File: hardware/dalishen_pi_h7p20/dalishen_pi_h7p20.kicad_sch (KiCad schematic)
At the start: 100 parts, among them J1 Conn_02x05_Odd_Even, J6 5V, J7 OV5640, J9 D500C930SV0, SW1 SW_Push, SW2 SW_Push, SW3 SW_DIP_x03, U3 H7P20N0L128-M3H1, U4 SY7201ABC, U5 XC6206-2.8, U7 P25Q32SH-SSH-IT, U8 XC6206-1.5, X1 NC

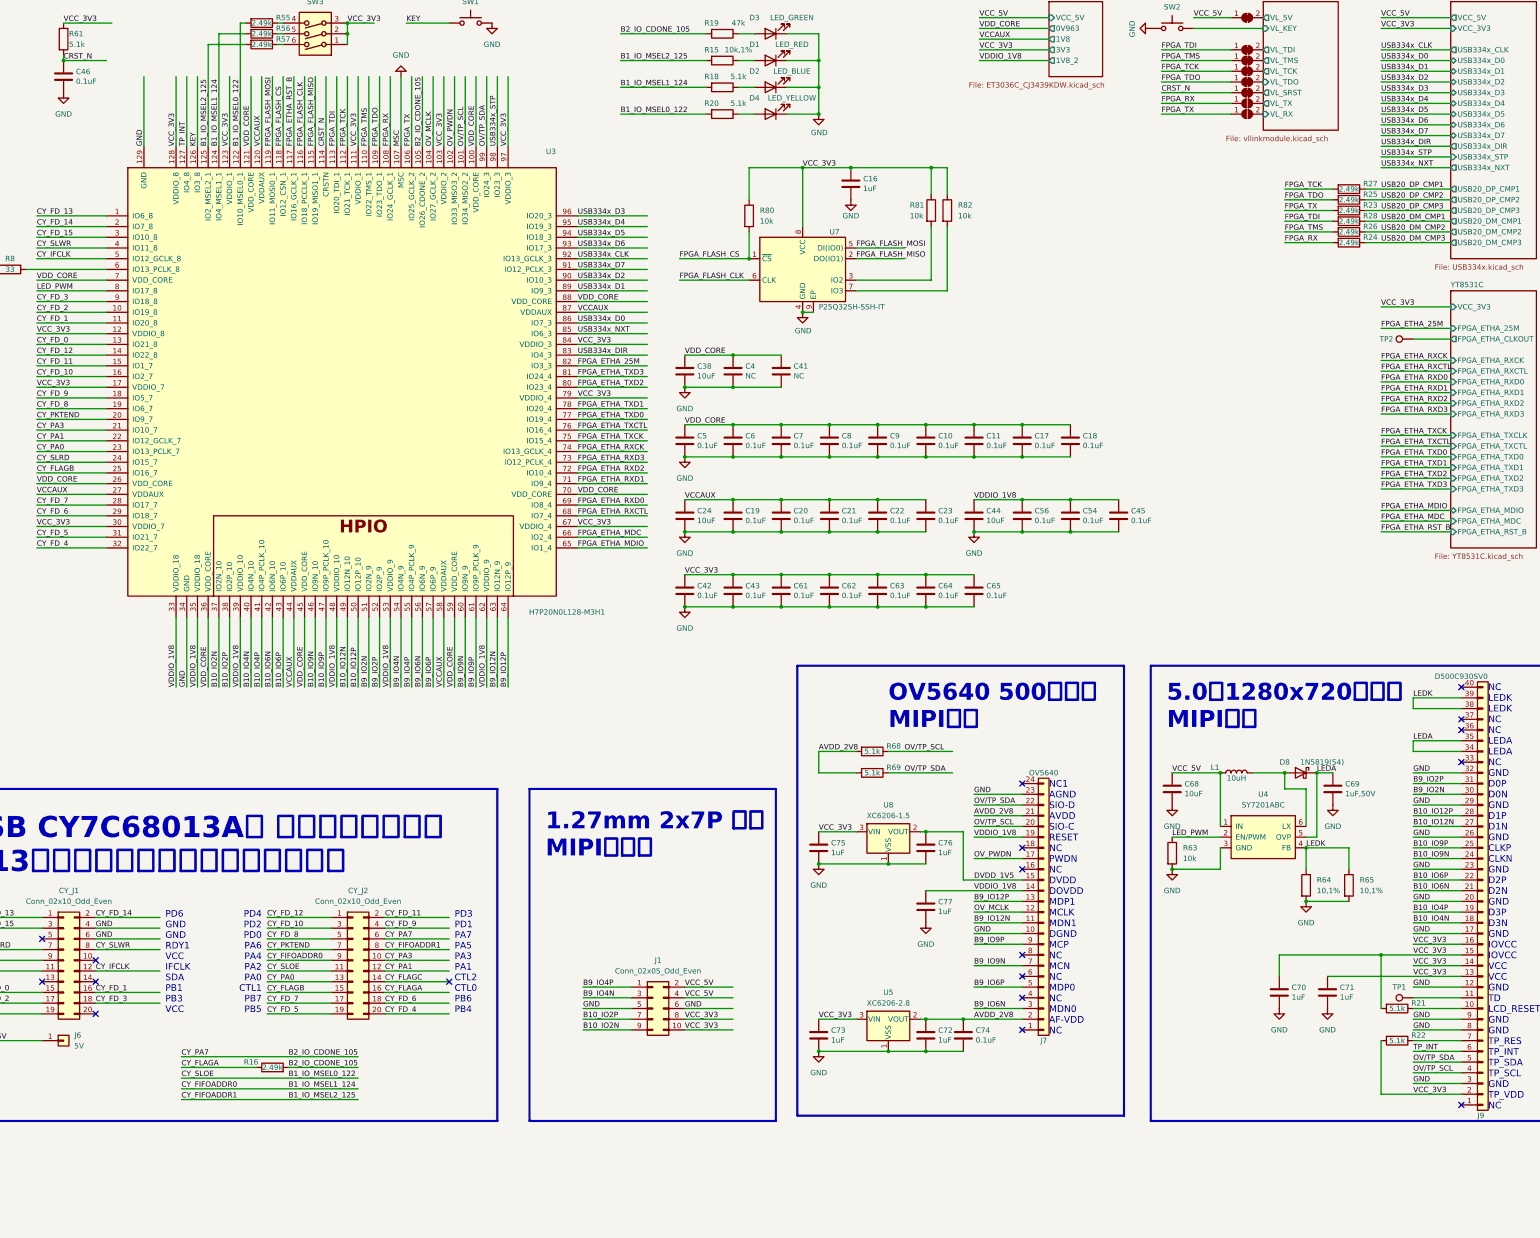
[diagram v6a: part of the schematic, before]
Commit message: [dalishen_pi_h7p20] CRST电容增大、MIPI CSI使用同一bank
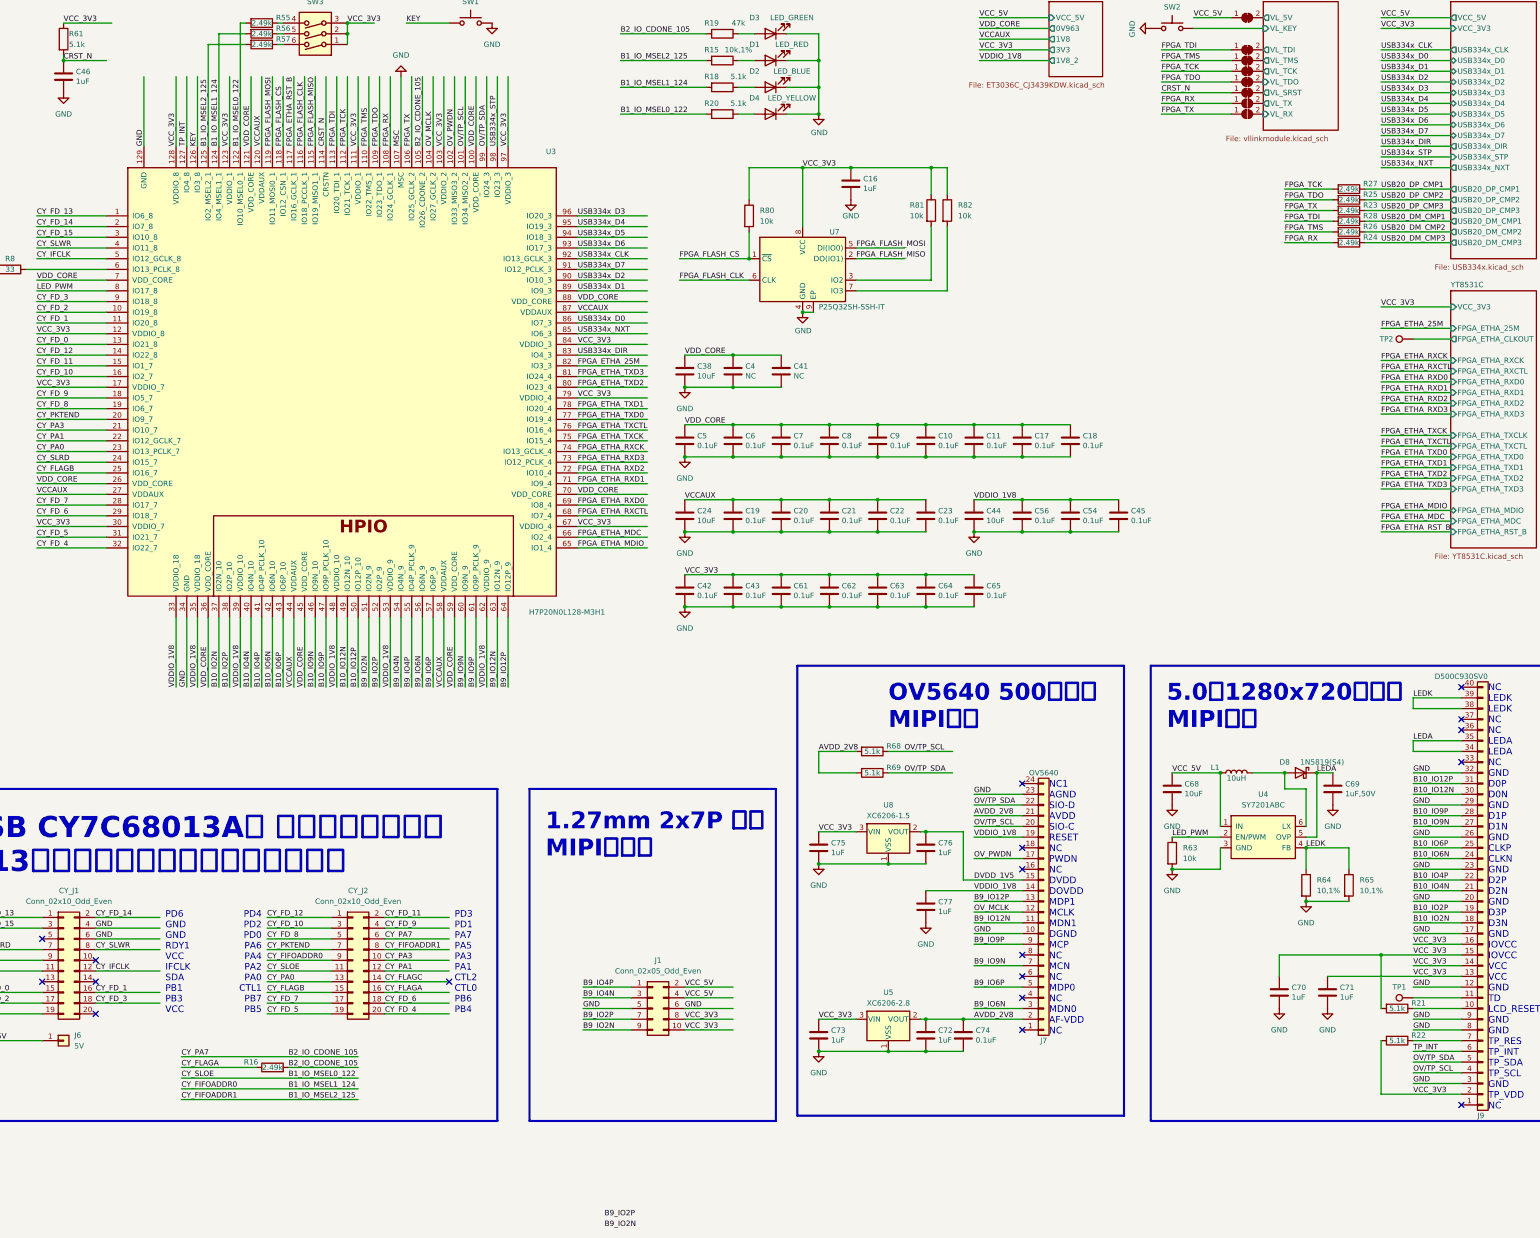
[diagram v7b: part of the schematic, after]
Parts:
- C46: value 0.1uF -> 1uF
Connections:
- net B10_IO12N: now also J9.30 (Pin_30); no longer J9.27 (Pin_27)
- net B10_IO12P: now also J9.31 (Pin_31); no longer J9.28 (Pin_28)
- net B10_IO2N: now also J9.18 (Pin_18); no longer J1.9 (Pin_9)
- net B10_IO2P: now also J9.19 (Pin_19); no longer J1.7 (Pin_7)
- net B10_IO4N: now also J9.21 (Pin_21); no longer J9.18 (Pin_18)
- net B10_IO4P: now also J9.22 (Pin_22); no longer J9.19 (Pin_19)
- net B10_IO6N: now also J9.24 (Pin_24); no longer J9.21 (Pin_21)
- net B10_IO6P: now also J9.25 (Pin_25); no longer J9.22 (Pin_22)
- net B10_IO9N: now also J9.27 (Pin_27); no longer J9.24 (Pin_24)
- net B10_IO9P: now also J9.28 (Pin_28); no longer J9.25 (Pin_25)
- net B9_IO2N: now also J1.9 (Pin_9); no longer J9.30 (Pin_30)
- net B9_IO2P: now also J1.7 (Pin_7); no longer J9.31 (Pin_31)
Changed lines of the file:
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@@
     (effects (font (size 1.27 1.27)) (justify left bottom))
   )
-  (label "B10_IO4P" (at 374.65 232.41 0) (fields_autoplaced)
+  (label "B10_IO4P" (at 374.65 224.79 0) (fields_autoplaced)
     (effects (font (size 1.27 1.27)) (justify left bottom))
   )
-  (label "B9_IO2N" (at 374.65 204.47 0) (fields_autoplaced)
+  (label "B9_IO2N" (at 182.88 307.34 0) (fields_autoplaced)
     (effects (font (size 1.27 1.27)) (justify left bottom))
   )
@@
     (effects (font (size 1.27 1.27)) (justify left bottom))
   )
-  (label "B10_IO12P" (at 374.65 209.55 0) (fields_autoplaced)
+  (label "B10_IO12P" (at 374.65 201.93 0) (fields_autoplaced)
     (effects (font (size 1.27 1.27)) (justify left bottom))
   )
@@
     (effects (font (size 1.27 1.27)) (justify left bottom))
   )
+  (label "B9_IO2N" (at 177.8 260.35 0) (fields_autoplaced)
+    (effects (font (size 1.27 1.27)) (justify left bottom))
+  )
   (label "GND" (at 62.23 238.76 0) (fields_autoplaced)
     (effects (font (size 1.27 1.27)) (justify left bottom))
@@
     (effects (font (size 1.27 1.27)) (justify left bottom))
   )
-  (label "B10_IO6P" (at 374.65 224.79 0) (fields_autoplaced)
+  (label "B10_IO6P" (at 374.65 217.17 0) (fields_autoplaced)
     (effects (font (size 1.27 1.27)) (justify left bottom))
   )
@@
     (effects (font (size 1.27 1.27)) (justify left bottom))
   )
-  (label "B10_IO9P" (at 374.65 217.17 0) (fields_autoplaced)
+  (label "B10_IO9P" (at 374.65 209.55 0) (fields_autoplaced)
     (effects (font (size 1.27 1.27)) (justify left bottom))
   )
@@
     (effects (font (size 1.27 1.27)) (justify left bottom))
   )
+  (label "B9_IO2P" (at 177.8 257.81 0) (fields_autoplaced)
+    (effects (font (size 1.27 1.27)) (justify left bottom))
+  )
   (label "GND" (at 374.65 214.63 0) (fields_autoplaced)
     (effects (font (size 1.27 1.27)) (justify left bottom))
@@
     (effects (font (size 1.27 1.27)) (justify left bottom))
   )
-  (label "B10_IO6N" (at 374.65 227.33 0) (fields_autoplaced)
+  (label "B10_IO6N" (at 374.65 219.71 0) (fields_autoplaced)
     (effects (font (size 1.27 1.27)) (justify left bottom))
   )
@@
     (effects (font (size 1.27 1.27)) (justify left bottom))
   )
-  (label "B10_IO2N" (at 177.8 260.35 0) (fields_autoplaced)
+  (label "B10_IO2N" (at 374.65 234.95 0) (fields_autoplaced)
     (effects (font (size 1.27 1.27)) (justify left bottom))
   )
@@
     (effects (font (size 1.27 1.27)) (justify left bottom))
   )
-  (label "B10_IO4N" (at 374.65 234.95 0) (fields_autoplaced)
+  (label "B10_IO4N" (at 374.65 227.33 0) (fields_autoplaced)
     (effects (font (size 1.27 1.27)) (justify left bottom))
   )
@@
     (effects (font (size 1.27 1.27)) (justify left bottom))
   )
-  (label "B10_IO12N" (at 374.65 212.09 0) (fields_autoplaced)
+  (label "B10_IO12N" (at 374.65 204.47 0) (fields_autoplaced)
     (effects (font (size 1.27 1.27)) (justify left bottom))
   )
@@
     (effects (font (size 1.27 1.27)) (justify left bottom))
   )
-  (label "B10_IO2P" (at 177.8 257.81 0) (fields_autoplaced)
+  (label "B10_IO2P" (at 374.65 232.41 0) (fields_autoplaced)
     (effects (font (size 1.27 1.27)) (justify left bottom))
   )
@@
     (effects (font (size 1.27 1.27)) (justify left bottom))
   )
-  (label "B9_IO2P" (at 374.65 201.93 0) (fields_autoplaced)
+  (label "B9_IO2P" (at 182.88 304.8 0) (fields_autoplaced)
     (effects (font (size 1.27 1.27)) (justify left bottom))
   )
@@
     (effects (font (size 1.27 1.27)) (justify left bottom))
   )
-  (label "B10_IO9N" (at 374.65 219.71 0) (fields_autoplaced)
+  (label "B10_IO9N" (at 374.65 212.09 0) (fields_autoplaced)
     (effects (font (size 1.27 1.27)) (justify left bottom))
   )
@@
       (effects (font (size 1.27 1.27)) (justify right))
     )
-    (property "Value" "0.1uF" (at 57.531 35.433 0)
+    (property "Value" "1uF" (at 57.531 35.433 0)
       (effects (font (size 1.27 1.27)) (justify right))
     )

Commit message: [dalishen_pi_h7p20] layout done
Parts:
- added R11, R9: 33, Resistor_SMD:R_0402_1005Metric, symbol Device:R
- added SW4, SW5: SW_Push, vllogic:SW-3x6mm_Hxx_SMD, symbol Switch:SW_Push
- R19: value 47k -> 10k,1%
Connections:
- net B9_IO4N: now also R9.2
- net B9_IO4P: now also R11.2
- net FPGA_ETHA_MDC: now also U3.81 (IO24_4); no longer U3.66 (IO2_4)
- net FPGA_ETHA_MDIO: now also U3.73 (IO12_PCLK_4); no longer U3.65 (IO1_4)
- net FPGA_ETHA_RXCTL: now also U3.75 (IO15_4); no longer U3.68 (IO7_4)
- net FPGA_ETHA_RXD0: now also U3.76 (IO16_4); no longer U3.69 (IO8_4)
- net FPGA_ETHA_RXD1: now also U3.77 (IO19_4); no longer U3.71 (IO9_4)
- net FPGA_ETHA_RXD2: now also U3.78 (IO20_4); no longer U3.72 (IO10_4)
- net FPGA_ETHA_RXD3: now also U3.80 (IO23_4); no longer U3.73 (IO12_PCLK_4)
- net FPGA_ETHA_TXCK: now also U3.65 (IO1_4); no longer U3.75 (IO15_4)
- net FPGA_ETHA_TXCTL: now also U3.66 (IO2_4); no longer U3.76 (IO16_4)
- net FPGA_ETHA_TXD0: now also U3.68 (IO7_4); no longer U3.77 (IO19_4)
- net FPGA_ETHA_TXD1: now also U3.69 (IO8_4); no longer U3.78 (IO20_4)
- net FPGA_ETHA_TXD2: now also U3.71 (IO9_4); no longer U3.80 (IO23_4)
- net FPGA_ETHA_TXD3: now also U3.72 (IO10_4); no longer U3.81 (IO24_4)
- net GND: now also SW4.2, SW5.2
- net OV_MCLK: now also R11.1; no longer U3.104 (IO27_GCLK_2)
- net OV_PWDN: now also R9.1; no longer U3.102 (IO33_MISO3_2)
- net VCCAUX: no longer C21.2
- net VDDIO_1V8: now also C21.2
- net KEY renamed KEY0
- new net KEY1: SW4.1, U3.104 (IO27_GCLK_2)
- new net KEY2: SW5.1, U3.102 (IO33_MISO3_2)
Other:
- note added: "OV/TP_SCL：可置0或高阻 OV/TP_SDA：可置0或高阻 OV_PWDN：可置0或高阻"
- moved on the sheet: C10, C11, C17, C18, C19, C20, C21, C22, C23, C24, C38, C4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
